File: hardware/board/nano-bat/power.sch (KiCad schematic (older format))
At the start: 19 parts

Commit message: Adding larger microcontroller
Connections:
- net labels removed: Enable
- wire segments 88 -> 89
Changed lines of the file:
@@
 encoding utf-8
 Sheet 2 6
-Title ""
+Title "NanoBat"
 Date ""
-Rev ""
-Comp ""
-Comment1 ""
+Rev "0.1.0"
+Comp "Vertigo Designs"
+Comment1 "Author: Ryan Summers"
 Comment2 ""
 Comment3 ""
@@
 Text HLabel 1550 3250 0    50   Input ~ 0
 Pgood
-Text HLabel 1550 3050 0    50   Input ~ 0
-Enable
 Wire Wire Line
 	2100 2850 2100 3450
@@
 	2250 5550 1800 5550
 Wire Wire Line
-	1800 5550 1800 1700
+	1800 5550 1800 3050
 Connection ~ 2250 5550
 Connection ~ 1800 1700
@@
 Wire Wire Line
 	1550 3250 2500 3250
-Wire Wire Line
-	1550 3050 2500 3050
 Wire Wire Line
 	1550 1700 1800 1700
@@
 	3200 5500 3200 5550
 Connection ~ 3200 5550
+Wire Wire Line
+	1800 3050 2500 3050
+Connection ~ 1800 3050
+Wire Wire Line
+	1800 3050 1800 1700
 $EndSCHEMATC

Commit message: Adding WIP before reverting
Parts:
- removed U?: L78L33_SO8, Package_SO:SOIC-8_3.9x4.9mm_P1.27mm, symbol Regulator_Linear:L78L33_SO8
- added FB?: Ferrite_Bead, symbol Device:Ferrite_Bead
- added U?: MCP1702, Package_TO_SOT_SMD:SOT-23, symbol Regulator_Linear:MCP1703A-2802_SOT23
- C?: value .33u -> 1u
- C?: value .1u -> 1u
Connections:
- net labels added: +2V8
- net labels removed: +3.3V
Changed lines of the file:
@@
 $Descr A4 11693 8268
 encoding utf-8
-Sheet 2 6
+Sheet 2 5
 Title "NanoBat"
 Date ""
@@
 U 1 1 5DD600C1
 P 4400 3450
-F 0 "R?" V 4195 3450 50  0000 C CNN
-F 1 "R_US" V 4286 3450 50  0000 C CNN
+F 0 "R?" V 4500 3400 50  0000 C CNN
+F 1 "R_US" V 4600 3450 50  0000 C CNN
 F 2 "" V 4440 3440 50  0001 C CNN
 F 3 "~" H 4400 3450 50  0001 C CNN
@@
 Wire Wire Line
 	6550 3250 6800 3250
-Text HLabel 7000 2850 2    50   Input ~ 0
+Text HLabel 7300 2850 2    50   Input ~ 0
 Vsoc
 Wire Wire Line
@@
 	6650 2750 6250 2750
 $Comp
-L Regulator_Linear:L78L33_SO8 U?
-U 1 1 5DDF2722
-P 2750 5550
-F 0 "U?" H 2750 5792 50  0000 C CNN
-F 1 "L78L33_SO8" H 2750 5701 50  0000 C CNN
-F 2 "Package_SO:SOIC-8_3.9x4.9mm_P1.27mm" H 2850 5750 50  0001 C CIN
-F 3 "http://www.st.com/content/ccc/resource/technical/document/datasheet/15/55/e5/aa/23/5b/43/fd/CD00000446.pdf/files/CD00000446.pdf/jcr:content/translations/en.CD00000446.pdf" H 2950 5550 50  0001 C CNN
-	1    2750 5550
-	1    0    0    -1
-$EndComp
-$Comp
 L Device:C C?
 U 1 1 5DDF31C7
 P 2250 5750
 F 0 "C?" H 2365 5796 50  0000 L CNN
-F 1 ".33u" H 2365 5705 50  0000 L CNN
+F 1 "1u" H 2365 5705 50  0000 L CNN
 F 2 "" H 2288 5600 50  0001 C CNN
 F 3 "~" H 2250 5750 50  0001 C CNN
@@
 P 3200 5750
 F 0 "C?" H 3315 5796 50  0000 L CNN
-F 1 ".1u" H 3315 5705 50  0000 L CNN
+F 1 "1u" H 3315 5705 50  0000 L CNN
 F 2 "" H 3238 5600 50  0001 C CNN
 F 3 "~" H 3200 5750 50  0001 C CNN
@@
 Wire Wire Line
 	1550 1700 1800 1700
-$Comp
-L power:+3.3V #PWR?
-U 1 1 5DE15BA9
+Wire Wire Line
+	3200 5500 3200 5550
+Connection ~ 3200 5550
+Wire Wire Line
+	1800 3050 2500 3050
+Connection ~ 1800 3050
+Wire Wire Line
+	1800 3050 1800 1700
+$Comp
+L Device:Ferrite_Bead FB?
+U 1 1 5DDC9F96
+P 7150 2850
+F 0 "FB?" V 6876 2850 50  0000 C CNN
+F 1 "Ferrite_Bead" V 6967 2850 50  0000 C CNN
+F 2 "" V 7080 2850 50  0001 C CNN
+F 3 "~" H 7150 2850 50  0001 C CNN
+	1    7150 2850
+	0    1    1    0
+$EndComp
+$Comp
+L Regulator_Linear:MCP1703A-2802_SOT23 U?
+U 1 1 5DDCE1EA
+P 2750 5550
+F 0 "U?" H 2750 5792 50  0000 C CNN
+F 1 "MCP1702" H 2750 5701 50  0000 C CNN
+F 2 "Package_TO_SOT_SMD:SOT-23" H 2750 5750 50  0001 C CNN
+F 3 "http://ww1.microchip.com/downloads/en/DeviceDoc/20005122B.pdf" H 2750 5500 50  0001 C CNN
+	1    2750 5550
+	1    0    0    -1
+$EndComp
+$Comp
+L power:+2V8 #PWR?
+U 1 1 5DDCF7B0
 P 3200 5500
 F 0 "#PWR?" H 3200 5350 50  0001 C CNN
-F 1 "+3.3V" H 3215 5673 50  0000 C CNN
+F 1 "+2V8" H 3215 5673 50  0000 C CNN
 F 2 "" H 3200 5500 50  0001 C CNN
 F 3 "" H 3200 5500 50  0001 C CNN
@@
 	1    0    0    -1
 $EndComp
-Wire Wire Line
-	3200 5500 3200 5550
-Connection ~ 3200 5550
-Wire Wire Line
-	1800 3050 2500 3050
-Connection ~ 1800 3050
-Wire Wire Line
-	1800 3050 1800 1700
 $EndSCHEMATC

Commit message: Adding complete schematic
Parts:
- removed D?: D_Zener_ALT, symbol Device:D_Zener_ALT
- removed Q?: Q_PMOS_DGS, symbol Device:Q_PMOS_DGS
- added C?: 10u, symbol Device:C
- added D?: D_Schottky_ALT, symbol Device:D_Schottky_ALT
- added Q?: Q_NMOS_DGS, symbol Device:Q_NMOS_DGS
- added R?: 10k, symbol Device:R_US
- C? (x3): value C -> .1u
- C? (x2): value C -> 4.7u
- C?: value C -> 10u
- L?: value L -> 37.5u
- R?: value R_US -> 2.2k
- R?: value R_US -> 95.3k
- R?: value R_US -> 15k
- R?: value R_US -> 3.925k
- R?: value R_US -> 10.5k
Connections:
- wire segments 89 -> 95
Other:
- note added: "DNI"
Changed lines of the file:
@@
-$EndComp
-$Comp
-L Device:Q_PMOS_DGS Q?
-U 1 1 5DD5C74B
-P 4550 2600
-F 0 "Q?" H 4756 2646 50  0000 L CNN
-F 1 "Q_PMOS_DGS" H 4756 2555 50  0000 L CNN
-F 2 "" H 4750 2700 50  0001 C CNN
-F 3 "~" H 4550 2600 50  0001 C CNN
-	1    4550 2600
-	1    0    0    -1
 $EndComp
 $Comp
@@
 P 5700 2850
 F 0 "L?" V 5890 2850 50  0000 C CNN
-F 1 "L" V 5799 2850 50  0000 C CNN
+F 1 "37.5u" V 5799 2850 50  0000 C CNN
 F 2 "" H 5700 2850 50  0001 C CNN
 F 3 "~" H 5700 2850 50  0001 C CNN
@@
 P 5350 2550
 F 0 "C?" H 5465 2596 50  0000 L CNN
-F 1 "C" H 5465 2505 50  0000 L CNN
+F 1 ".1u" H 5465 2505 50  0000 L CNN
 F 2 "" H 5388 2400 50  0001 C CNN
 F 3 "~" H 5350 2550 50  0001 C CNN
@@
 P 6400 3050
 F 0 "C?" H 6515 3096 50  0000 L CNN
-F 1 "C" H 6515 3005 50  0000 L CNN
+F 1 ".1u" H 6515 3005 50  0000 L CNN
 F 2 "" H 6438 2900 50  0001 C CNN
 F 3 "~" H 6400 3050 50  0001 C CNN
@@
 P 4400 3450
 F 0 "R?" V 4500 3400 50  0000 C CNN
-F 1 "R_US" V 4600 3450 50  0000 C CNN
+F 1 "2.2k" V 4600 3450 50  0000 C CNN
 F 2 "" V 4440 3440 50  0001 C CNN
 F 3 "~" H 4400 3450 50  0001 C CNN
@@
 P 5350 3650
 F 0 "R?" H 5282 3604 50  0000 R CNN
-F 1 "R_US" H 5282 3695 50  0000 R CNN
+F 1 "95.3k" H 5282 3695 50  0000 R CNN
 F 2 "" V 5390 3640 50  0001 C CNN
 F 3 "~" H 5350 3650 50  0001 C CNN
@@
 P 6000 3050
 F 0 "R?" H 5932 3004 50  0000 R CNN
-F 1 "R_US" H 5932 3095 50  0000 R CNN
+F 1 "15k" H 5932 3095 50  0000 R CNN
 F 2 "" V 6040 3040 50  0001 C CNN
 F 3 "~" H 6000 3050 50  0001 C CNN
@@
 P 6000 3450
 F 0 "R?" H 5932 3404 50  0000 R CNN
-F 1 "R_US" H 5932 3495 50  0000 R CNN
+F 1 "3.925k" H 5932 3495 50  0000 R CNN
 F 2 "" V 6040 3440 50  0001 C CNN
 F 3 "~" H 6000 3450 50  0001 C CNN
@@
 P 5350 4000
 F 0 "C?" H 5465 4046 50  0000 L CNN
-F 1 "C" H 5465 3955 50  0000 L CNN
+F 1 ".1u" H 5465 3955 50  0000 L CNN
 F 2 "" H 5388 3850 50  0001 C CNN
 F 3 "~" H 5350 4000 50  0001 C CNN
@@
 P 2050 1900
 F 0 "C?" H 2165 1946 50  0000 L CNN
-F 1 "C" H 2165 1855 50  0000 L CNN
+F 1 "4.7u" H 2165 1855 50  0000 L CNN
 F 2 "" H 2088 1750 50  0001 C CNN
 F 3 "~" H 2050 1900 50  0001 C CNN
@@
 P 2100 2650
 F 0 "C?" H 2215 2696 50  0000 L CNN
-F 1 "C" H 2215 2605 50  0000 L CNN
+F 1 "4.7u" H 2215 2605 50  0000 L CNN
 F 2 "" H 2138 2500 50  0001 C CNN
 F 3 "~" H 2100 2650 50  0001 C CNN
@@
 Wire Wire Line
 	3100 3950 3100 3900
-$Comp
-L Device:D_Zener_ALT D?
-U 1 1 5DD7377D
-P 3000 1800
-F 0 "D?" H 3000 1584 50  0000 C CNN
-F 1 "D_Zener_ALT" H 3000 1675 50  0000 C CNN
-F 2 "" H 3000 1800 50  0001 C CNN
-F 3 "~" H 3000 1800 50  0001 C CNN
-	1    3000 1800
-	-1   0    0    1
-$EndComp
 Wire Wire Line
 	4350 2450 4350 2350
@@
 P 6800 3050
 F 0 "C?" H 6915 3096 50  0000 L CNN
-F 1 "C" H 6915 3005 50  0000 L CNN
+F 1 "10u" H 6915 3005 50  0000 L CNN
 F 2 "" H 6838 2900 50  0001 C CNN
 F 3 "~" H 6800 3050 50  0001 C CNN
@@
 L power:GND #PWR?
 U 1 1 5DD91B2B
-P 6550 3300
-F 0 "#PWR?" H 6550 3050 50  0001 C CNN
-F 1 "GND" H 6555 3127 50  0000 C CNN
-F 2 "" H 6550 3300 50  0001 C CNN
-F 3 "" H 6550 3300 50  0001 C CNN
-	1    6550 3300
-	1    0    0    -1
-$EndComp
-$Comp
-L power:GNDPWR #PWR?
-U 1 1 5DD91F5C
 P 6800 3300
-F 0 "#PWR?" H 6800 3100 50  0001 C CNN
-F 1 "GNDPWR" H 6804 3146 50  0000 C CNN
-F 2 "" H 6800 3250 50  0001 C CNN
-F 3 "" H 6800 3250 50  0001 C CNN
+F 0 "#PWR?" H 6800 3050 50  0001 C CNN
+F 1 "GND" H 6805 3127 50  0000 C CNN
+F 2 "" H 6800 3300 50  0001 C CNN
+F 3 "" H 6800 3300 50  0001 C CNN
 	1    6800 3300
 	1    0    0    -1
@@
 	6800 3200 6800 3250
 Connection ~ 6800 3250
-Wire Wire Line
-	6800 3250 6800 3300
-Wire Wire Line
-	6550 3300 6550 3250
-Wire Wire Line
-	6550 3250 6800 3250
-Text HLabel 7300 2850 2    50   Input ~ 0
+Text HLabel 7750 2850 2    50   Input ~ 0
 Vsoc
-Wire Wire Line
-	7000 2850 6800 2850
 Connection ~ 6800 2850
-Text HLabel 1550 3250 0    50   Input ~ 0
+Text HLabel 1250 3250 0    50   Input ~ 0
 Pgood
 Wire Wire Line
@@
 P 2100 4200
 F 0 "R?" V 1895 4200 50  0000 C CNN
-F 1 "R_US" V 1986 4200 50  0000 C CNN
+F 1 "10.5k" V 1986 4200 50  0000 C CNN
 F 2 "" V 2140 4190 50  0001 C CNN
 F 3 "~" H 2100 4200 50  0001 C CNN
@@
 	1550 4200 1950 4200
 Wire Wire Line
-	1550 3250 2500 3250
-Wire Wire Line
 	1550 1700 1800 1700
 Wire Wire Line
@@
 L Device:Ferrite_Bead FB?
 U 1 1 5DDC9F96
-P 7150 2850
-F 0 "FB?" V 6876 2850 50  0000 C CNN
-F 1 "Ferrite_Bead" V 6967 2850 50  0000 C CNN
-F 2 "" V 7080 2850 50  0001 C CNN
-F 3 "~" H 7150 2850 50  0001 C CNN
-	1    7150 2850
+P 7600 2850
+F 0 "FB?" V 7326 2850 50  0000 C CNN
+F 1 "Ferrite_Bead" V 7417 2850 50  0000 C CNN
+F 2 "" V 7530 2850 50  0001 C CNN
+F 3 "~" H 7600 2850 50  0001 C CNN
+	1    7600 2850
 	0    1    1    0
 $EndComp
@@
 	1    0    0    -1
 $EndComp
+$Comp
+L Device:D_Schottky_ALT D?
+U 1 1 5E4F96BB
+P 3000 1800
+F 0 "D?" H 3000 1584 50  0000 C CNN
+F 1 "D_Schottky_ALT" H 3000 1675 50  0000 C CNN
+F 2 "" H 3000 1800 50  0001 C CNN
+F 3 "~" H 3000 1800 50  0001 C CNN
+	1    3000 1800
+	-1   0    0    1
+$EndComp
+$Comp
+L Device:R_US R?
+U 1 1 5E4FADC8
+P 1350 3000
+F 0 "R?" H 1418 3046 50  0000 L CNN
+F 1 "10k" H 1418 2955 50  0000 L CNN
+F 2 "" V 1390 2990 50  0001 C CNN
+F 3 "~" H 1350 3000 50  0001 C CNN
+	1    1350 3000
+	1    0    0    -1
+$EndComp
+$Comp
+L power:+2V8 #PWR?
+U 1 1 5E4FB40E
+P 1350 2800
+F 0 "#PWR?" H 1350 2650 50  0001 C CNN
+F 1 "+2V8" H 1365 2973 50  0000 C CNN
+F 2 "" H 1350 2800 50  0001 C CNN
+F 3 "" H 1350 2800 50  0001 C CNN
+	1    1350 2800
+	1    0    0    -1
+$EndComp
+Wire Wire Line
+	1350 3150 1350 3250
+Wire Wire Line
+	1350 3250 2500 3250
+Wire Wire Line
+	1350 3250 1250 3250
+Connection ~ 1350 3250
+Wire Wire Line
+	1350 2850 1350 2800
+$Comp
+L Device:Q_NMOS_DGS Q?
+U 1 1 5E503A75
+P 4550 2600
+F 0 "Q?" H 4756 2646 50  0000 L CNN
+F 1 "Q_NMOS_DGS" H 4756 2555 50  0000 L CNN
+F 2 "" H 4750 2700 50  0001 C CNN
+F 3 "~" H 4550 2600 50  0001 C CNN
+	1    4550 2600
+	1    0    0    -1
+$EndComp
+$Comp
+L Device:C C?
+U 1 1 5E507FF0
+P 7150 3050
+F 0 "C?" H 7265 3096 50  0000 L CNN
+F 1 "10u" H 7265 3005 50  0000 L CNN
+F 2 "" H 7188 2900 50  0001 C CNN
+F 3 "~" H 7150 3050 50  0001 C CNN
+	1    7150 3050
+	1    0    0    -1
+$EndComp
+Wire Wire Line
+	7150 2900 7150 2850
+Wire Wire Line
+	6800 2850 7150 2850
+Wire Wire Line
+	7150 3250 6800 3250
+Wire Wire Line
+	7150 2850 7450 2850
+Connection ~ 7150 2850
+Wire Wire Line
+	7150 3200 7150 3250
+Wire Wire Line
+	6800 3250 6800 3300
+$Comp
+L power:GNDPWR #PWR?
+U 1 1 5DD91F5C
+P 7150 3300
+F 0 "#PWR?" H 7150 3100 50  0001 C CNN
+F 1 "GNDPWR" H 7154 3146 50  0000 C CNN
+F 2 "" H 7150 3250 50  0001 C CNN
+F 3 "" H 7150 3250 50  0001 C CNN
+	1    7150 3300
+	1    0    0    -1
+$EndComp
+Wire Wire Line
+	7150 3300 7150 3250
+Connection ~ 7150 3250
+Text Notes 5600 4150 0    50   ~ 0
+DNI
+Text Notes 5600 3850 0    50   ~ 0
+DNI
 $EndSCHEMATC

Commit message: Adding first-pass revisions and annotations, part selection
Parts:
- removed C? (x3): .1u, symbol Device:C
- removed C? (x2): 4.7u, symbol Device:C
- removed C? (x2): 10u, symbol Device:C
- removed C? (x2): 1u, symbol Device:C
- removed FB?: Ferrite_Bead, symbol Device:Ferrite_Bead
- removed Q? (x2): Q_NMOS_DGS, symbol Device:Q_NMOS_DGS
- removed R?: 2.2k, symbol Device:R_US
- removed R?: 10k, symbol Device:R_US
- added C501, C504, C507, C508, C509: 0.1u, Capacitor_SMD:C_0603_1608Metric, symbol Device:C
- added C502, C510: 4.7u, Capacitor_SMD:C_0603_1608Metric, symbol Device:C
- added C503, C505, C506: 1u, Capacitor_SMD:C_0603_1608Metric, symbol Device:C
- added NT501: Net-Tie_2, NetTie:NetTie-2_SMD_Pad2.0mm, symbol Device:Net-Tie_2
- added Q501: Q_PMOS_GSD, Package_TO_SOT_SMD:SOT-23, symbol Device:Q_PMOS_GSD
- added Q502, Q503: Q_NMOS_GSD, Package_TO_SOT_SMD:SOT-23, symbol Device:Q_NMOS_GSD
- added R501, R502, R503: 10k, Resistor_SMD:R_0603_1608Metric, symbol Device:R_US
- added R504: 2.2k, Resistor_SMD:R_0603_1608Metric, symbol Device:R_US
- D501: renamed from D?; footprint (none) -> Diode_SMD:D_SOD-323; Part (none) -> BAT54HT1GOSCT-ND
- L501: renamed from L?; value 37.5u -> 50u; footprint (none) -> footprints:NRS6028-IND-NS; Part (none) -> 587-2942-1-ND
- R505: renamed from R?; footprint (none) -> Resistor_SMD:R_0603_1608Metric; Part (none) -> P95.3KDBCT-ND
- R506: renamed from R?; footprint (none) -> Resistor_SMD:R_0603_1608Metric; Part (none) -> P15KDBCT-ND
- R507: renamed from R?; value 3.925k -> 3.9k; footprint (none) -> Resistor_SMD:R_0603_1608Metric; Part (none) -> P3.9KDBCT-ND
- R508: renamed from R?; footprint (none) -> Resistor_SMD:R_0603_1608Metric; Part (none) -> P10.5KDBCT-ND
- U501: renamed from U?; footprint MLF-16_ML_4X4 -> footprints:MIC2104YML-TR; Part (none) -> 576-4157-1-ND
- U502: renamed from U?; Part (none) -> MCP1702T-3302E/CBCT-ND
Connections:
- net labels added: En, Vext
- wire segments 95 -> 97
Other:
- note removed: "DNI"
- moved on the sheet: D501, L501, R505, R506, R507, R508, U501, U502

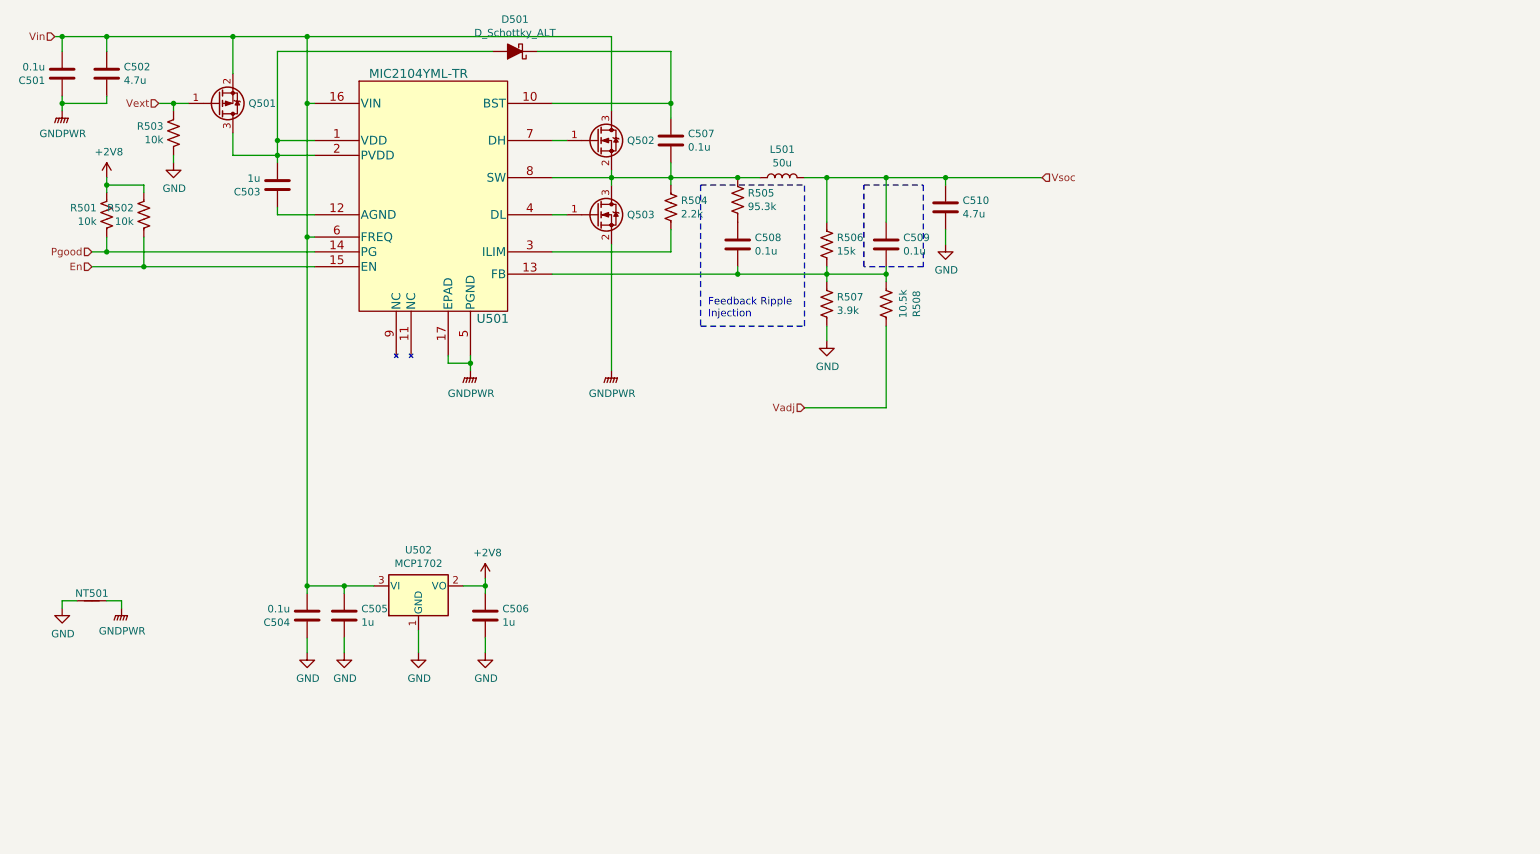
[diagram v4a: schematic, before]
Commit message: Adding 3D models, reorg, minor schematic fixes
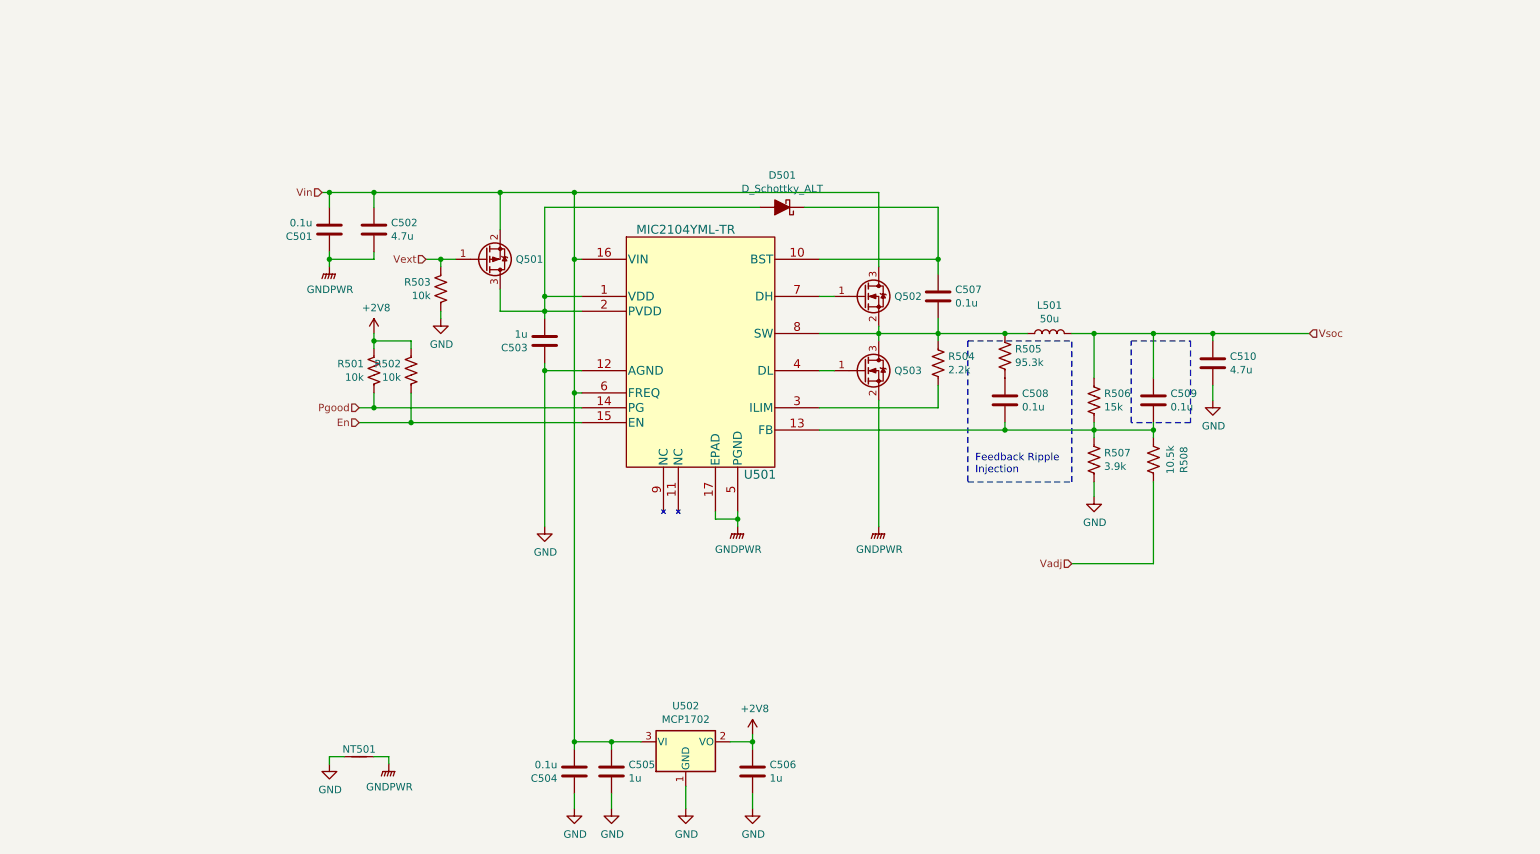
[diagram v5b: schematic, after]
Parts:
- U501: footprint footprints:MIC2104YML-TR -> Package_DFN_QFN:QFN-16-1EP_3x3mm_P0.5mm_EP1.7x1.7mm
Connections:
- net GND: now also C503.1, U501.12 (AGND)
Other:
- moved on the sheet: C501, C502, C503, C504, C505, C506, C507, C508, C509, C510, D501, L501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
